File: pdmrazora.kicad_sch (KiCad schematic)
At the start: 2 parts, among them J1 SuperSeal26_Razor, J2 M6_VBAT_GND

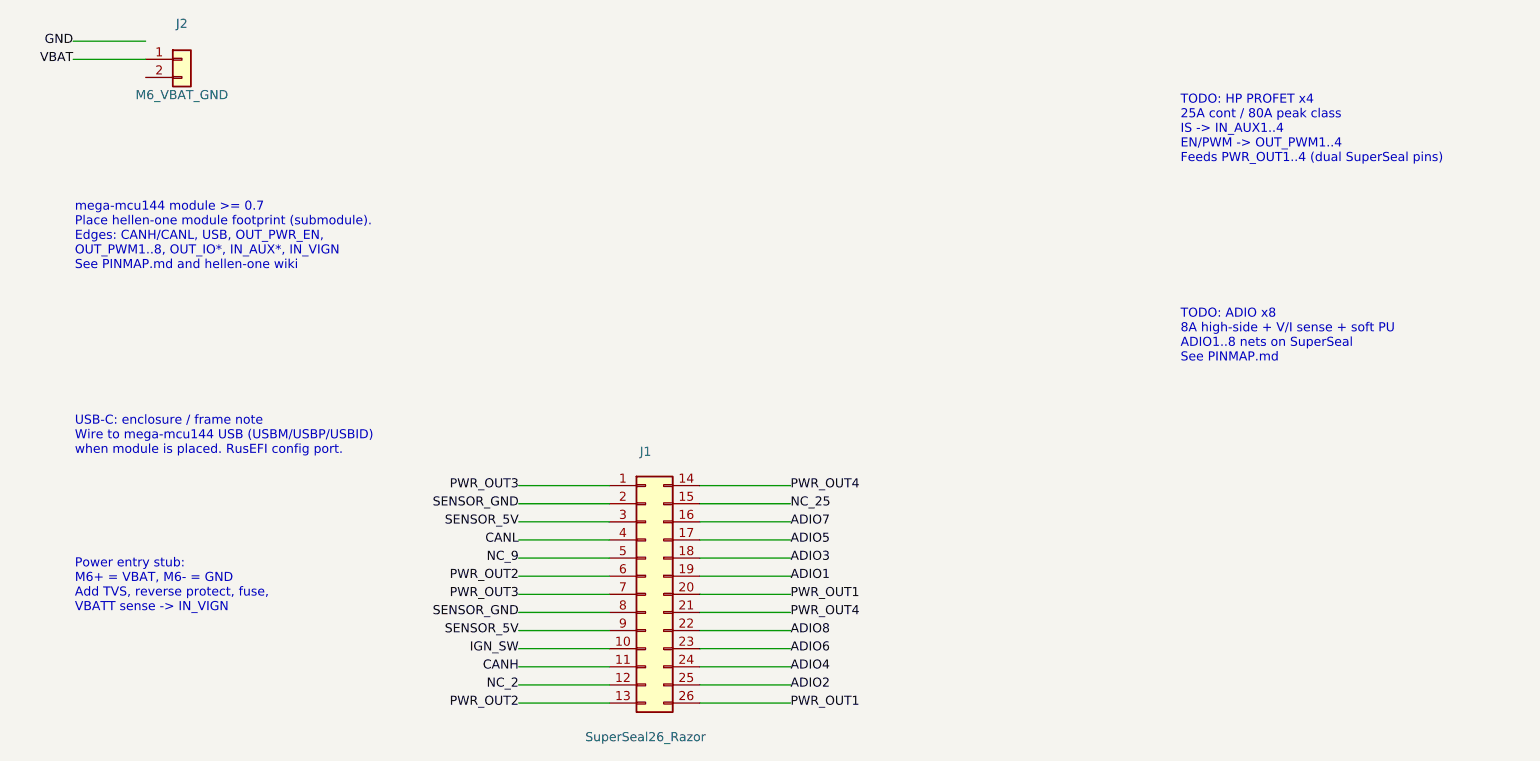
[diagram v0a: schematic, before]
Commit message: Place mega-mcu144 0.7 and stub HP PROFET x4 / ADIO x8 stages
Put the 0.7 module on the 160x120 mm frame (M1000, 0°), wire PINMAP edge labels to Razor SuperSeal nets, and replace schematic TODOs with HP/ADIO hierarchical sheets (PN TBD).
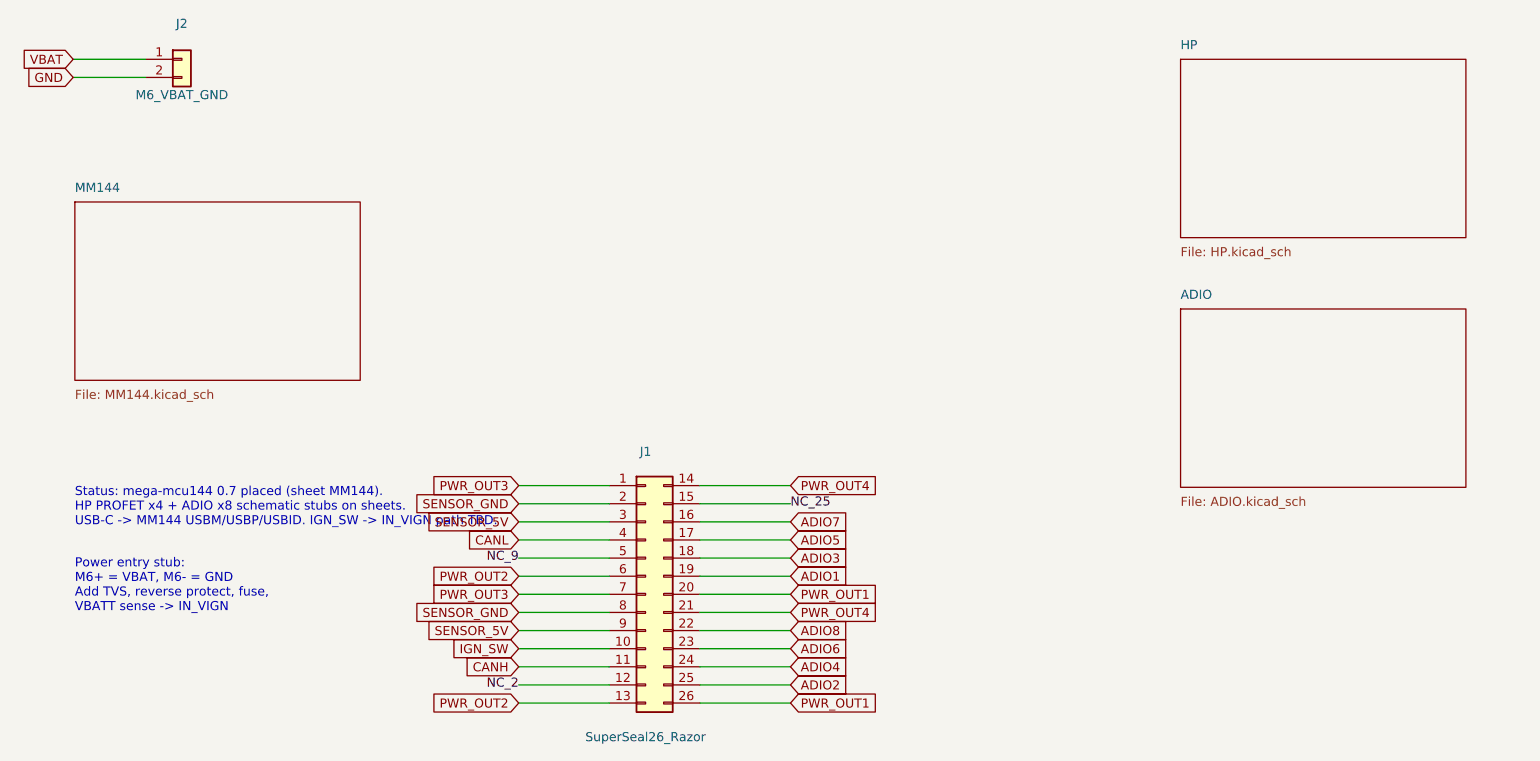
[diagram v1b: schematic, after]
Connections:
- net GND: now also J2.2 (Pin_2)
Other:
- added sheet ADIO (ADIO.kicad_sch)
- added sheet HP (HP.kicad_sch)
- added sheet MM144 (MM144.kicad_sch)
- note added: "Status: mega-mcu144 0.7 placed (sheet MM144). HP PROFET x4 + ADIO x8 schematic stubs on sheets. USB-C -> MM144 USBM/USBP/USBID. IGN_SW -> IN_VIGN path TBD."
- note removed: "TODO: ADIO x8 8A high-side + V/I sense + soft PU ADIO1..8 nets on SuperSeal See PINMAP.md"
- note removed: "TODO: HP PROFET x4 25A cont / 80A peak class IS -> IN_AUX1..4 EN/PWM -> OUT_PWM1..4 Feeds PWR_OUT1..4 (dual SuperSeal pins)"
- note removed: "USB-C: enclosure / frame note Wire to mega-mcu144 USB (USBM/USBP/USBID) when module is placed. RusEFI config port."
- note removed: "mega-mcu144 module >= 0.7 Place hellen-one module footprint (submodule). Edges: CANH/CANL, USB, OUT_PWR_EN, OUT_PWM1..8, OUT_IO*, IN_AUX*, IN_VIGN See PINMAP.md and hellen-one wiki"
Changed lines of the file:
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@@
 		)
 	)
-	(label "PWR_OUT2"
+	(global_label "PWR_OUT2"
 		(at 82.22 125.24 0)
+		(shape input)
 		(effects
 			(font
@@
 		)
 	)
-	(label "CANH"
+	(global_label "CANH"
 		(at 82.22 120.16 0)
+		(shape input)
 		(effects
 			(font
@@
 		)
 	)
-	(label "IGN_SW"
+	(global_label "IGN_SW"
 		(at 82.22 117.62 0)
+		(shape input)
 		(effects
 			(font
@@
 		)
 	)
-	(label "SENSOR_5V"
+	(global_label "SENSOR_5V"
 		(at 82.22 115.08 0)
+		(shape input)
 		(effects
 			(font
@@
 		)
 	)
-	(label "SENSOR_GND"
+	(global_label "SENSOR_GND"
 		(at 82.22 112.54 0)
+		(shape input)
 		(effects
 			(font
@@
 		)
 	)
-	(label "PWR_OUT3"
+	(global_label "PWR_OUT3"
 		(at 82.22 110.0 0)
+		(shape input)
 		(effects
 			(font
@@
 		)
 	)
-	(label "PWR_OUT2"
+	(global_label "PWR_OUT2"
 		(at 82.22 107.46 0)
+		(shape input)
 		(effects
 			(font
@@
 		)
 	)
-	(label "CANL"
+	(global_label "CANL"
 		(at 82.22 102.38 0)
+		(shape input)
 		(effects
 			(font
@@
 		)
 	)
-	(label "SENSOR_5V"
+	(global_label "SENSOR_5V"
 		(at 82.22 99.84 0)
+		(shape input)
 		(effects
 			(font
@@
 		)
 	)
-	(label "SENSOR_GND"
+	(global_label "SENSOR_GND"
 		(at 82.22 97.3 0)
+		(shape input)
 		(effects
 			(font
@@
 		)
 	)
-	(label "PWR_OUT3"
+	(global_label "PWR_OUT3"
 		(at 82.22 94.76 0)
+		(shape input)
 		(effects
 			(font
@@
 		)
 	)
-	(label "PWR_OUT1"
+	(global_label "PWR_OUT1"
 		(at 120.32000000000001 125.24 0)
+		(shape input)
 		(effects
 			(font
@@
 		)
 	)
-	(label "ADIO2"
+	(global_label "ADIO2"
 		(at 120.32000000000001 122.7 0)
+		(shape input)
 		(effects
 			(font
@@
 		)
 	)
-	(label "ADIO4"
+	(global_label "ADIO4"
 		(at 120.32000000000001 120.16 0)
+		(shape input)
 		(effects
 			(font
@@
 		)
 	)
-	(label "ADIO6"
+	(global_label "ADIO6"
 		(at 120.32000000000001 117.62 0)
+		(shape input)
 		(effects
 			(font
@@
 		)
 	)
-	(label "ADIO8"
+	(global_label "ADIO8"
 		(at 120.32000000000001 115.08 0)
+		(shape input)
 		(effects
 			(font
@@
 		)
 	)
-	(label "PWR_OUT4"
+	(global_label "PWR_OUT4"
 		(at 120.32000000000001 112.54 0)
+		(shape input)
 		(effects
 			(font
@@
 		)
 	)
-	(label "PWR_OUT1"
+	(global_label "PWR_OUT1"
 		(at 120.32000000000001 110.0 0)
+		(shape input)
 		(effects
 			(font
@@
 		)
 	)
-	(label "ADIO1"
+	(global_label "ADIO1"
 		(at 120.32000000000001 107.46 0)
+		(shape input)
 		(effects
 			(font
@@
 		)
 	)
-	(label "ADIO3"
+	(global_label "ADIO3"
 		(at 120.32000000000001 104.92 0)
+		(shape input)
 		(effects
 			(font
@@
 		)
 	)
-	(label "ADIO5"
+	(global_label "ADIO5"
 		(at 120.32000000000001 102.38 0)
+		(shape input)
 		(effects
 			(font
@@
 		)
 	)
-	(label "ADIO7"
+	(global_label "ADIO7"
 		(at 120.32000000000001 99.84 0)
+		(shape input)
 		(effects
 			(font
@@
 		)
 	)
-	(label "PWR_OUT4"
+	(global_label "PWR_OUT4"
 		(at 120.32000000000001 94.76 0)
+		(shape input)
 		(effects
 			(font
@@
 		)
 	)
-	(label "VBAT"
+	(global_label "VBAT"
 		(at 19.76 35.0 0)
-		(effects
-			(font
-				(size 1.27 1.27)
-			)
-			(justify right)
-		)
-	)
-	(wire
-		(pts
-			(xy 29.92 32.46) (xy 19.76 32.46)
-		)
-		(stroke
-			(width 0)
-			(type default)
-		)
-	)
-	(label "GND"
-		(at 19.76 32.46 0)
-		(effects
-			(font
-				(size 1.27 1.27)
-			)
-			(justify right)
-		)
-	)
-	(text "mega-mcu144 module >= 0.7\nPlace hellen-one module footprint (submodule).\nEdges: CANH/CANL, USB, OUT_PWR_EN,\nOUT_PWM1..8, OUT_IO*, IN_AUX*, IN_VIGN\nSee PINMAP.md and hellen-one wiki"
-		(exclude_from_sim no)
-		(at 20 55 0)
-		(effects
-			(font
-				(size 1.27 1.27)
-			)
-			(justify left top)
-		)
-	)
-	(text "TODO: HP PROFET x4\n25A cont / 80A peak class\nIS -> IN_AUX1..4\nEN/PWM -> OUT_PWM1..4\nFeeds PWR_OUT1..4 (dual SuperSeal pins)"
-		(exclude_from_sim no)
-		(at 175 40 0)
-		(effects
-			(font
-				(size 1.27 1.27)
-			)
-			(justify left top)
-		)
-	)
-	(text "TODO: ADIO x8\n8A high-side + V/I sense + soft PU\nADIO1..8 nets on SuperSeal\nSee PINMAP.md"
-		(exclude_from_sim no)
-		(at 175 70 0)
-		(effects
-			(font
-				(size 1.27 1.27)
-			)
-			(justify left top)
-		)
-	)
-	(text "USB-C: enclosure / frame note\nWire to mega-mcu144 USB (USBM/USBP/USBID)\nwhen module is placed. RusEFI config port."
-		(exclude_from_sim no)
-		(at 20 85 0)
-		(effects
-			(font
-				(size 1.27 1.27)
-			)
-			(justify left top)
+		(shape input)
+		(effects
+			(font
+				(size 1.27 1.27)
+			)
+			(justify right)
+		)
+	)
+	(wire
+		(pts
+			(xy 29.92 37.54) (xy 19.76 37.54)
+		)
+		(stroke
+			(width 0)
+			(type default)
+		)
+	)
+	(global_label "GND"
+		(at 19.76 37.54 0)
+		(shape input)
+		(effects
+			(font
+				(size 1.27 1.27)
+			)
+			(justify right)
 		)
 	)
@@
 		)
 	)
+	(text "Status: mega-mcu144 0.7 placed (sheet MM144).\nHP PROFET x4 + ADIO x8 schematic stubs on sheets.\nUSB-C -> MM144 USBM/USBP/USBID. IGN_SW -> IN_VIGN path TBD."
+		(exclude_from_sim no)
+		(at 20 95 0)
+		(effects
+			(font
+				(size 1.27 1.27)
+			)
+			(justify left top)
+		)
+	)
+	(sheet
+		(at 20 55)
+		(size 40 25)
+		(stroke
+			(width 0.1524)
+			(type solid)
+		)
+		(fill
+			(color 0 0 0 0.0000)
+		)
+		(exclude_from_sim no)
+		(in_bom yes)
+		(on_board yes)
+		(dnp no)
+		(property "Sheetname" "MM144"
+			(at 20 53.73 0)
+			(effects
+				(font
+					(size 1.27 1.27)
+				)
+				(justify left bottom)
+			)
+		)
+		(property "Sheetfile" "MM144.kicad_sch"
+			(at 20 81.27 0)
+			(effects
+				(font
+					(size 1.27 1.27)
+				)
+				(justify left top)
+			)
+		)
+	)
+	(sheet
+		(at 175 35)
+		(size 40 25)
+		(stroke
+			(width 0.1524)
+			(type solid)
+		)
+		(fill
+			(color 0 0 0 0.0000)
+		)
+		(exclude_from_sim no)
+		(in_bom yes)
+		(on_board yes)
+		(dnp no)
+		(property "Sheetname" "HP"
+			(at 175 33.73 0)
+			(effects
+				(font
+					(size 1.27 1.27)
+				)
+				(justify left bottom)
+			)
+		)
+		(property "Sheetfile" "HP.kicad_sch"
+			(at 175 61.27 0)
+			(effects
+				(font
+					(size 1.27 1.27)
+				)
+				(justify left top)
+			)
+		)
+	)
+	(sheet
+		(at 175 70)
+		(size 40 25)
+		(stroke
+			(width 0.1524)
+			(type solid)
+		)
+		(fill
+			(color 0 0 0 0.0000)
+		)
+		(exclude_from_sim no)
+		(in_bom yes)
+		(on_board yes)
+		(dnp no)
+		(property "Sheetname" "ADIO"
+			(at 175 68.73 0)
+			(effects
+				(font
+					(size 1.27 1.27)
+				)
+				(justify left bottom)
+			)
+		)
+		(property "Sheetfile" "ADIO.kicad_sch"
+			(at 175 96.27 0)
+			(effects
+				(font
+					(size 1.27 1.27)
+				)
+				(justify left top)
+			)
+		)
+	)
 	(sheet_instances
 		(path "/"
 			(page "1")
 		)
-	)
+		(path "/a1111111-1111-4111-a111-111111111111"
+			(page "2")
+		)
+		(path "/a2222222-2222-4222-a222-222222222222"
+			(page "3")
+		)
+		(path "/a3333333-3333-4333-a333-333333333333"
+			(page "4")
+		)
+	)

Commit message: Clear fab blockers 1–4: SuperSeal 9-6437287-8, PROFET PNs, power entry, PCB place
- Replace Conn_02x13 pin-header with TE/AMP SuperSeal 1.0 26-way
  (9-6437287-8, keying 1) via pdmrazora.pretty footprint (6473423-1 pattern)
- HP: keep BTS50010-1TAD; add RIS 2k7 + 10n; fix IN/IS wiring
- ADIO: BTS7004-1EPP; RIS 4k7 + soft PU 4k7 to SENSOR_5V; fix EN/IS wiring
- Power entry: fuse/TVS/bulk stubs + IGN_SW 100k/10k (~11:1) → IN_VIGN
- PCB: place SuperSeal, HP×4, ADIO×8 with nets; outline 180×140; thermal zones
- Document PNs, kILIS, AmpsPerVolt TODOs in HARDWARE_BOM.md / BOARD.md

Do not touch HELLCORE.
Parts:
- added C1: 100u_50V, Capacitor_SMD:C_1210_3225Metric, symbol Device:C
- added C2: 100n, Capacitor_SMD:C_0805_2012Metric, symbol Device:C
- added D1: SMBJ33CA, Diode_SMD:D_SMB, symbol Device:D
- added F1: 150A_MEGA_TBD, Fuse:Fuse_Holder_Blade_ATO, symbol Device:Fuse
- added R1: 100k, Resistor_SMD:R_0603_1608Metric, symbol Device:R
- added R2: 10k, Resistor_SMD:R_0603_1608Metric, symbol Device:R
- J1: value SuperSeal26_Razor -> 9-6437287-8; footprint Connector_PinHeader_2.54mm:PinHeader_2x13_P2.54mm_Vertical -> pdmrazora:TE_9-6437287-8_SuperSeal26
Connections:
- net GND: now also C1.1, C1.2, C2.1, C2.2, D1.2 (A), R2.2
- net IGN_SW: now also R1.1
- net VBAT: now also D1.1 (K)
- new net: R1.2, R2.1
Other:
- note added: "IGN_SW divider R1=100k / R2=10k (~11:1) into IN_VIGN (H144_IN_VBATT)."
- note added: "Reverse protect: ideal-diode/P-FET TBD. F1=Mega fuse TBD. D1=SMBJ33CA TVS. C1=100u C2=100n bulk stubs."
